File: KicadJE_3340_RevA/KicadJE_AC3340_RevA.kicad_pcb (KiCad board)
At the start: 2 copper layers, 200 x 128 mm, 147 parts, among them J101 RampOut1, J102 PulseOut2, J103 SawOut3, J104 In1.1, J105 In1.2, J106 In1.3, J107 SS_In2, J108 HS_In3, J109 FM_In4, J110 PWM_In5, J111 SineOut4, P101 HEADER_2x5_Doepfer, Q101 MMBT3906, Q102 UMX1N, SW101 Octave (3 state), U101 TL072, U102 TL072, U103 TL072, U104 AS3340, U105 L78L05_SOT89, U106 L79L05_SOT89, U107 TL072

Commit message: fix in sine section
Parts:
- moved R147 154.7 mm to (79.5, 145.8), turned to 90 degrees
- moved Q102 144.2 mm to (76.8, 140.2), turned to 270 degrees
- moved R137 140.4 mm to (79.5, 135.0), turned to 90 degrees
- moved R142 138.9 mm to (69.8, 136.5), turned to 90 degrees
- moved R143 135.2 mm to (79.8, 139.2)
- moved R141 125.9 mm to (73.5, 140.2), turned to 90 degrees
- moved R140 121.7 mm to (79.8, 141.2)
- moved RV104 108.9 mm to (69.8, 142.5), turned to 90 degrees
- moved R156 89.4 mm to (70.5, 88.5), turned to 180 degrees
- moved R144 78.7 mm to (88.8, 92.0), turned to 270 degrees
- moved RV103 72.6 mm to (87.0, 102.5), turned to 270 degrees
- moved D115 21.0 mm to (86.0, 156.5)
- moved U103 10.0 mm to (69.8, 130.0)
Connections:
- Q102 pad 6: Net-(Q102-Pad3) -> Net-(Q102-Pad6)
- R140 pad 1: Net-(Q102-Pad3) -> Net-(Q102-Pad6)
- R150 pad 1: Net-(Q102-Pad3) -> Net-(Q102-Pad6)
- U103 pad 6: Net-(Q102-Pad3) -> Net-(Q102-Pad6)
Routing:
- net Net-(Q102-Pad3): track 0.00 -> 17.7 mm
- net Net-(Q102-Pad4): track 0.00 -> 12.6 mm
- net Net-(R142-Pad1): track 0.00 -> 9.57 mm
- net +12VA: track 98.1 -> 90.1 mm
- net Net-(Q102-Pad1): track 0.00 -> 7.75 mm
- net Net-(Q102-Pad5): track 0.00 -> 7.26 mm
- net Net-(Q102-Pad2): track 0.00 -> 7.18 mm
- net -12VA: track 137.0 -> 132.7 mm
- net Net-(Q102-Pad6): track 0.00 -> 3.23 mm

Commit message: Protection Diodes
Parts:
- removed D111: 1N1007, Diode_SMD:D_SOD-123
- D109, D110, D113, D114: moved to F.Cu
- moved C103 145.0 mm to (52.0, 141.5), turned to 180 degrees
- moved R107 135.1 mm to (87.8, 135.0), turned to 180 degrees
- moved R153 130.0 mm to (87.7, 145.0)
- moved R112 128.1 mm to (52.0, 145.0)
- moved R116 126.4 mm to (87.8, 115.0), turned to 180 degrees
- moved C102 119.8 mm to (52.0, 135.0), turned to 180 degrees
- moved R111 119.7 mm to (52.0, 138.5)
- moved R113 119.7 mm to (52.0, 125.0)
- moved R152 118.5 mm to (15.7, 93.9)
- moved R162 118.0 mm to (21.0, 93.9)
- moved R135 116.9 mm to (20.8, 99.1)
- moved R127 116.9 mm to (15.5, 99.1)
- moved C101 114.6 mm to (52.0, 115.0)
- moved R102 114.2 mm to (10.4, 93.9)
- moved R139 114.1 mm to (26.2, 99.1)
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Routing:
- net +12VA: track 90.1 -> 122.6 mm, vias 2 -> 3
- net GND: track 26.6 -> 52.5 mm, vias 0 -> 2
- net 3FM_Lin_In4: track 0.00 -> 2.91 mm
- net -12VA: track 132.7 -> 133.4 mm

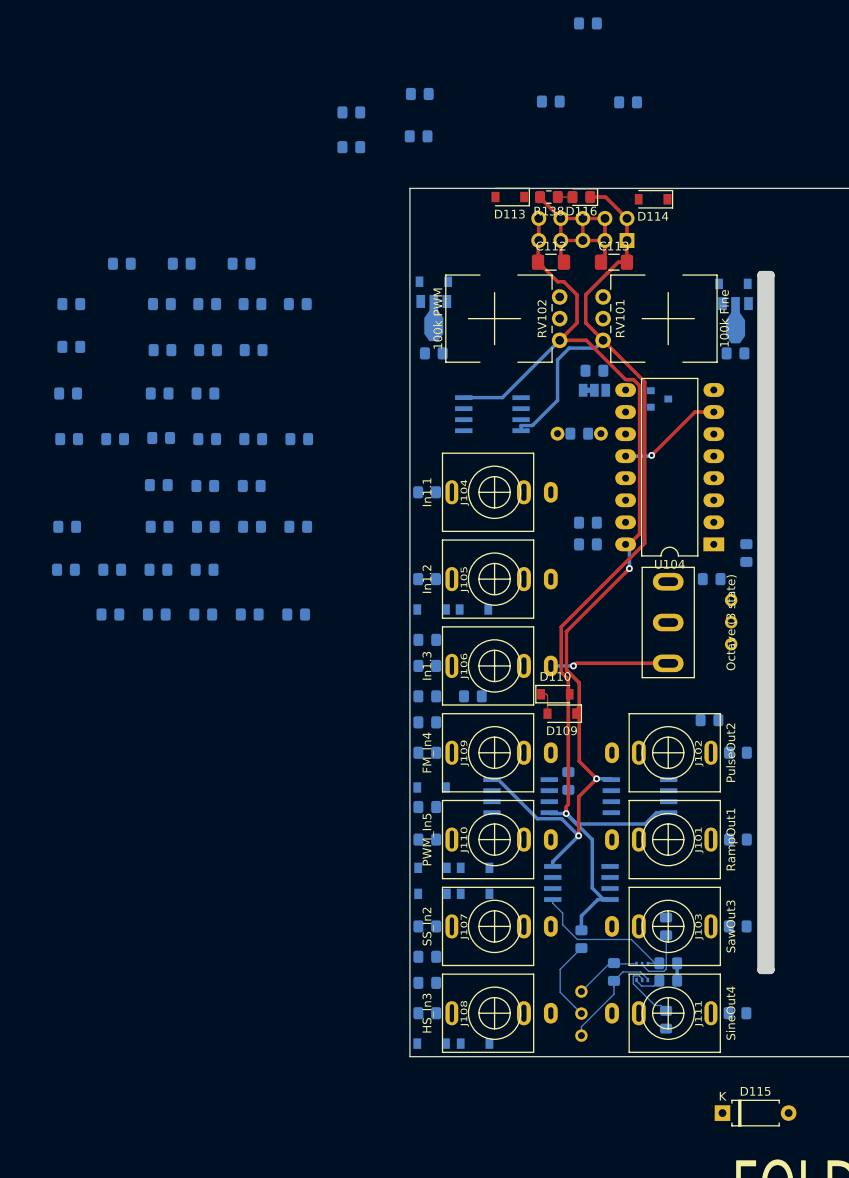
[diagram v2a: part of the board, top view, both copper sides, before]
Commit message: Update KicadJE_AC3340_RevA.kicad_pcb
All Capacitors placed
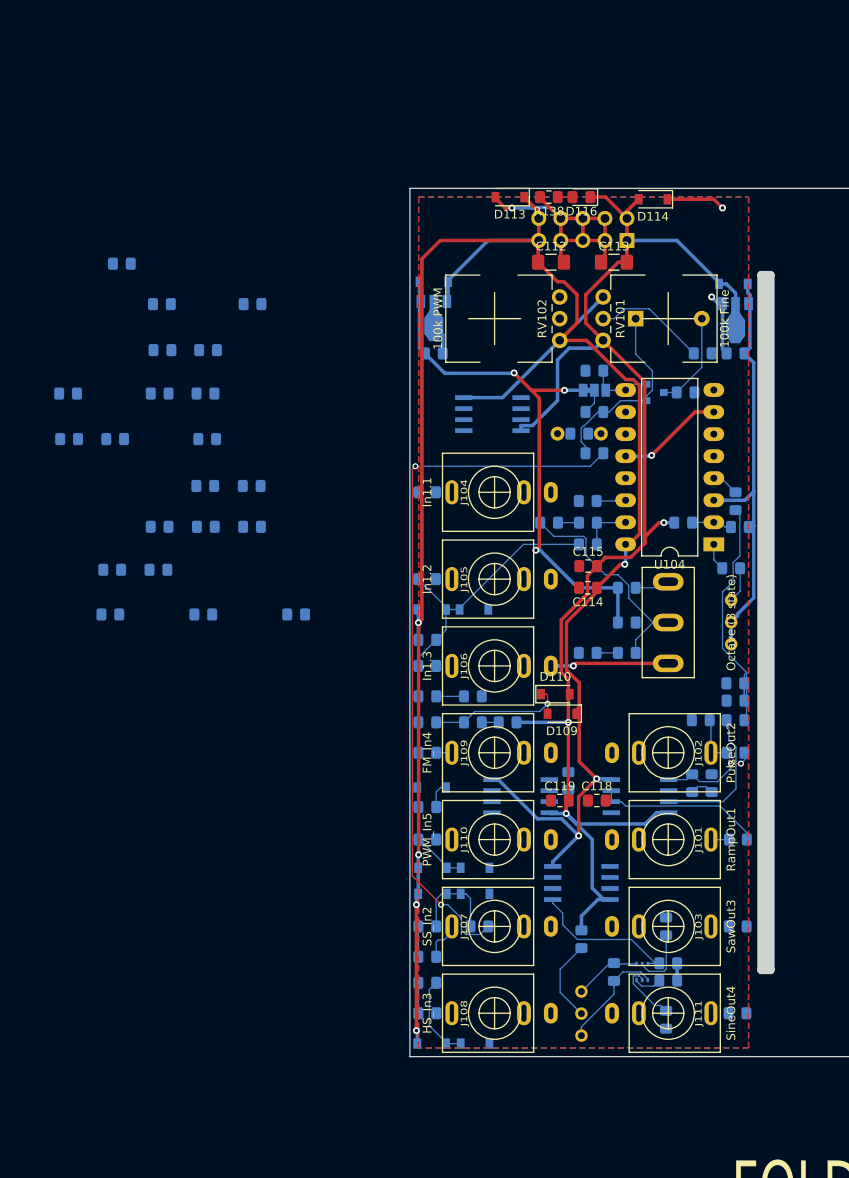
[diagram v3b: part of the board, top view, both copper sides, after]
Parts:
- C114, C115, C118, C119: moved to F.Cu
- D115: moved to B.Cu
- moved C107 95.4 mm to (58.0, 135.0), turned to 180 degrees
- moved D115 92.0 mm to (76.0, 65.0)
- moved C118 84.1 mm to (71.5, 120.5)
- moved C119 83.0 mm to (67.3, 120.5)
- moved R145 77.5 mm to (88.0, 89.0)
- moved R157 74.9 mm to (87.5, 107.0)
- moved R146 74.8 mm to (81.5, 88.5), turned to 180 degrees
- moved C105 72.8 mm to (61.2, 111.5), turned to 180 degrees
- moved R126 71.7 mm to (87.5, 111.2), turned to 180 degrees
- moved R103 71.4 mm to (75.0, 100.0), turned to 180 degrees
- moved R104 68.1 mm to (75.0, 103.5)
- moved R130 66.0 mm to (84.8, 118.5), turned to 270 degrees
- moved R120 61.3 mm to (82.5, 118.5), turned to 90 degrees
- moved R102 60.8 mm to (70.5, 103.5), turned to 180 degrees
- moved R125 59.2 mm to (57.2, 111.5), turned to 180 degrees
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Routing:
- net +12VA: track 122.6 -> 256.2 mm, vias 3 -> 7
- net Net-(C107-Pad1): track 0.00 -> 82.3 mm, vias 0 -> 2
- net +5V: track 0.00 -> 62.7 mm, vias 0 -> 3
- net -5V: track 0.00 -> 49.0 mm
- net -12VA: track 133.4 -> 169.2 mm, vias 1 -> 3
- net Net-(D103-Pad2): track 0.00 -> 34.7 mm
- net 3VP_2: track 0.00 -> 31.7 mm
- net GND: track 52.5 -> 79.0 mm, vias 2 -> 5
- net 3Octave: track 0.00 -> 25.8 mm
- net Net-(D115-Pad1): track 0.00 -> 22.5 mm
- net Net-(R105-Pad1): track 0.00 -> 19.1 mm
- net Net-(R126-Pad2): track 0.00 -> 16.6 mm
- net 3FM_Lin_In4: track 2.91 -> 16.6 mm, vias 0 -> 1
- net Net-(D101-Pad2): track 0.00 -> 13.7 mm
- net Net-(R119-Pad1): track 0.00 -> 13.0 mm
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- added copper zone on B.Cu, net GND
- added copper zone on F.Cu, net GND

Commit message: Update KicadJE_AC3340_RevA.kicad_pcb
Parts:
- moved R163 80.8 mm to (79.0, 129.5), turned to 90 degrees
- moved R150 77.3 mm to (64.0, 129.5), turned to 90 degrees
- moved R129 71.2 mm to (60.0, 115.2), turned to 90 degrees
- moved R152 69.8 mm to (75.8, 129.5), turned to 270 degrees
- moved R139 66.8 mm to (82.5, 135.0), turned to 270 degrees
- moved R134 63.2 mm to (70.2, 114.5), turned to 270 degrees
- moved R121 61.6 mm to (57.0, 119.5), turned to 90 degrees
- moved R132 52.6 mm to (70.2, 118.2), turned to 270 degrees
- moved R155 50.7 mm to (81.8, 75.8)
- moved R131 50.1 mm to (57.0, 124.0), turned to 90 degrees
- moved R124 43.2 mm to (64.2, 62.5)
- moved R133 42.8 mm to (64.2, 65.0), turned to 180 degrees
- moved R160 41.7 mm to (52.5, 78.8)
- moved R162 36.9 mm to (52.5, 74.8), turned to 180 degrees
- moved R123 35.9 mm to (59.8, 65.0)
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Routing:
- net Net-(C106-Pad1): track 3.07 -> 89.8 mm, vias 0 -> 6
- net 3HardSyncIn3: track 9.83 -> 96.2 mm, vias 0 -> 2
- net 3PWM_In5: track 0.00 -> 67.7 mm
- net Net-(R151-Pad1): track 2.42 -> 52.1 mm, vias 0 -> 4
- net Net-(R107-Pad1): track 0.00 -> 42.2 mm, vias 0 -> 2
- net +12VA: track 256.2 -> 295.6 mm
- net Net-(R150-Pad2): track 0.00 -> 38.2 mm
- net 3VTO_1: track 0.00 -> 33.5 mm, vias 0 -> 4
- net 3Octave: track 25.8 -> 55.3 mm, vias 0 -> 2
- net -5V: track 49.0 -> 75.6 mm, vias 0 -> 2
- net 3CVIn1: track 5.83 -> 32.3 mm
- net Net-(U104-Pad10): track 0.00 -> 24.1 mm
- net Net-(Q102-Pad6): track 3.23 -> 13.2 mm, vias 0 -> 2
- net Net-(R159-Pad2): track 0.00 -> 7.77 mm
- net 3VSO_3: track 7.35 -> 14.5 mm, vias 0 -> 2
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
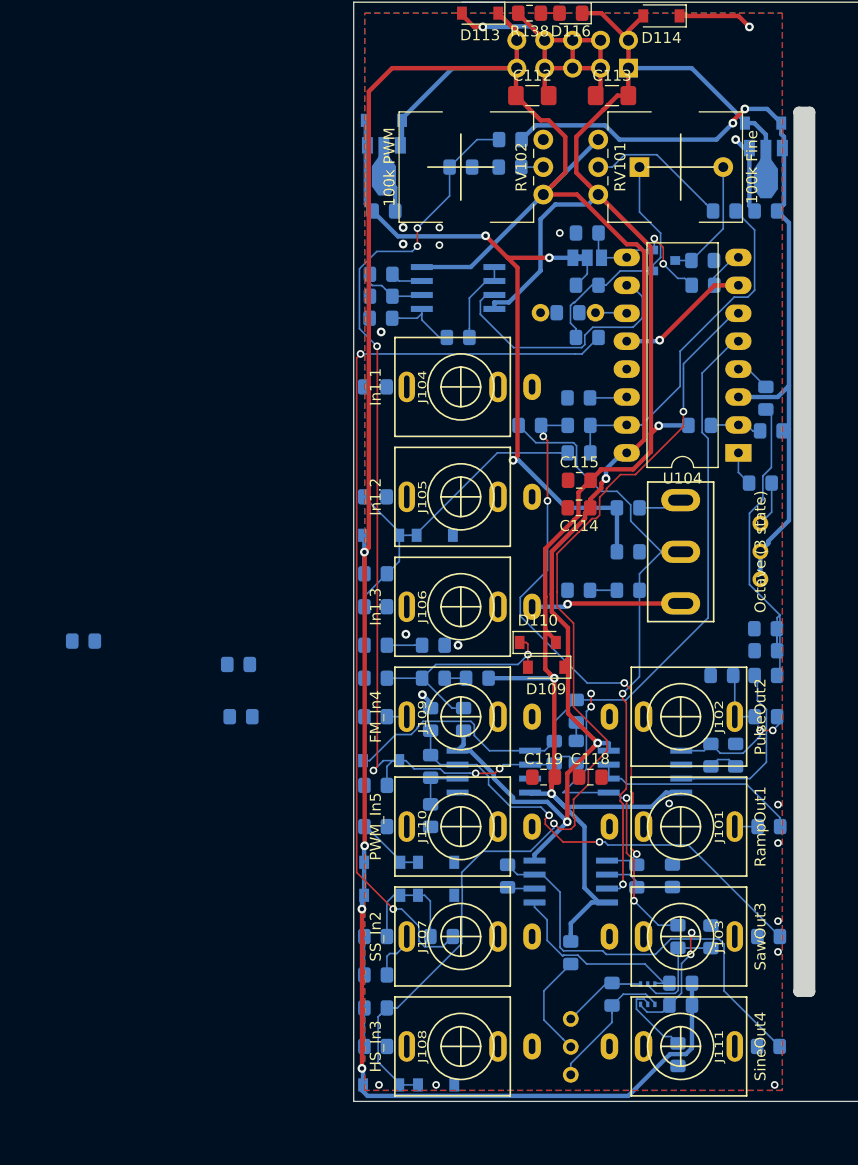
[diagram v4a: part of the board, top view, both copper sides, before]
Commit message: Update KicadJE_AC3340_RevA.kicad_pcb
Initial routing
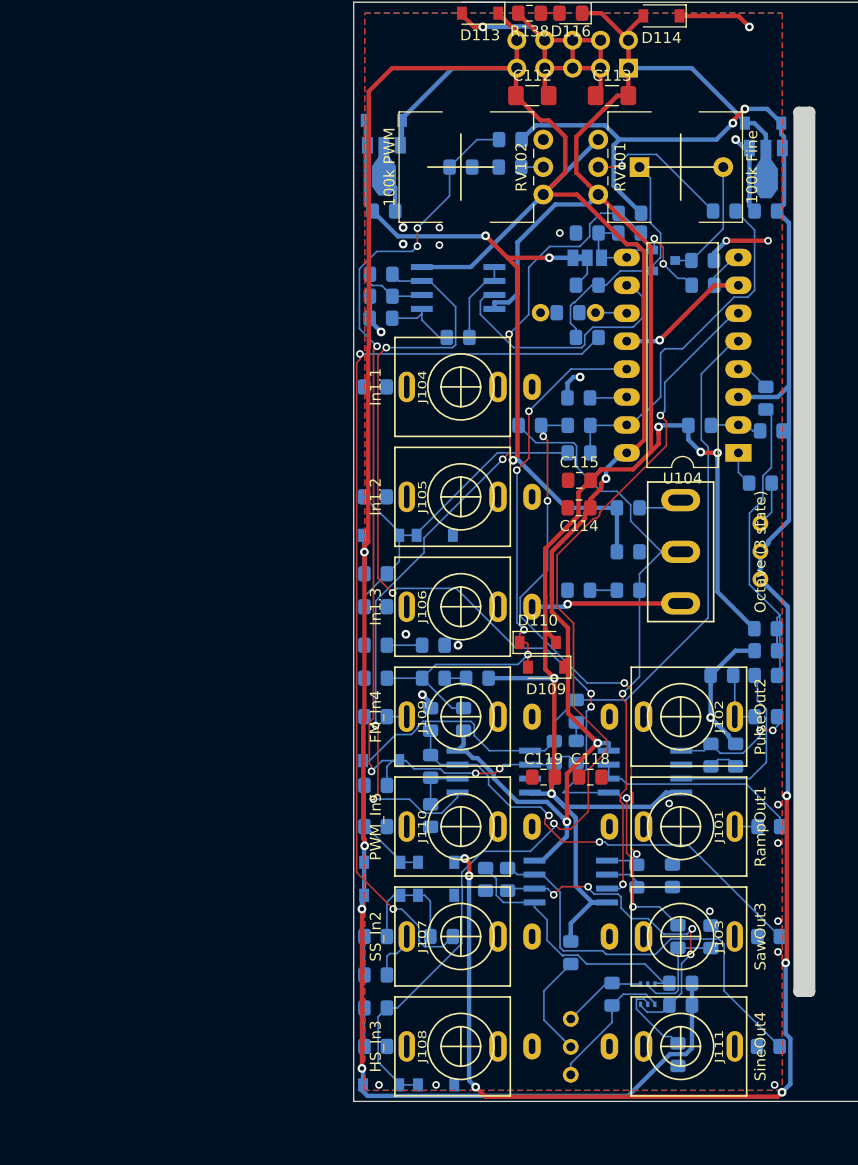
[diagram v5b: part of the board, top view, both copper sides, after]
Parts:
- moved R128 57.9 mm to (75.1, 69.2), turned to 180 degrees
- moved R127 53.0 mm to (75.1, 71.0)
- moved R149 42.5 mm to (62.0, 129.8), turned to 270 degrees
- moved R150 0.30 mm to (64.0, 129.8)
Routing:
- net -5V: track 75.6 -> 182.6 mm, vias 2 -> 8
- net Net-(R127-Pad2): track 0.00 -> 77.2 mm, vias 0 -> 4
- net 3VTO_1: track 33.5 -> 93.2 mm, vias 4 -> 6
- net 3FM_Lin_In4: track 21.5 -> 54.0 mm, vias 1 -> 4
- net GND: track 80.5 -> 105.1 mm, vias 22 -> 27
- net -12VA: track 171.3 -> 193.5 mm, vias 3 -> 5
- net Net-(Q102-Pad6): track 13.2 -> 31.1 mm, vias 2 -> 4
- net Net-(Q102-Pad3): track 18.1 -> 24.7 mm
- net 3VSO_3: track 14.5 -> 16.3 mm
- net 3HardSyncIn3: track 96.2 -> 95.7 mm
- net Net-(C106-Pad1): track 89.8 -> 90.3 mm
- net Net-(R119-Pad1): track 13.0 -> 13.3 mm, vias 0 -> 1
